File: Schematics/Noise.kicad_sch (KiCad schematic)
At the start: 110 parts, among them J81 Conn_01x02, J82 Conn_01x02, J83 Conn_01x02, J84 Conn_01x02, J85 Conn_01x03, J86 Conn_01x03, J89 Conn_01x03, Q1 2N3904, Q2 BSS138, Q7 BSS138, U126 LM1117-5, U63 TL074, U64 TL072, U65 DG212C, U66 DG212C, U67 TL074, U68 DG212C, U69 DG212C, U70 TL074, U71 PCF8575, U73 LM1117-3.3, U74 TL074, U75 TL074, U76 TL074

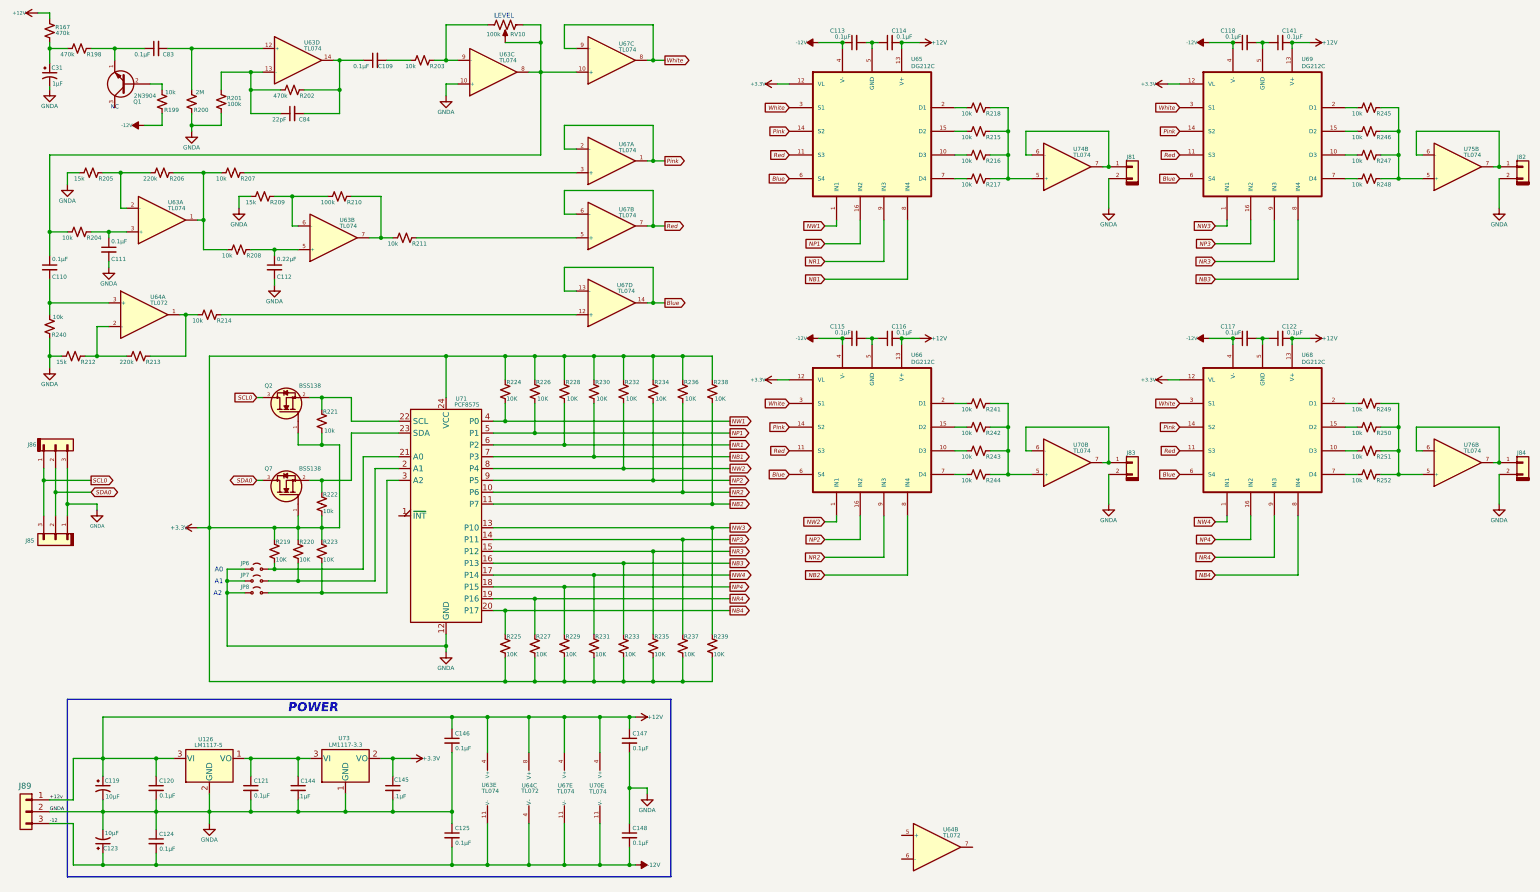
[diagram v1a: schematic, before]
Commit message: Upgreade byte value interface to short.  First stage of refactoring midi input for rotory encoders.  Still needs scaling.
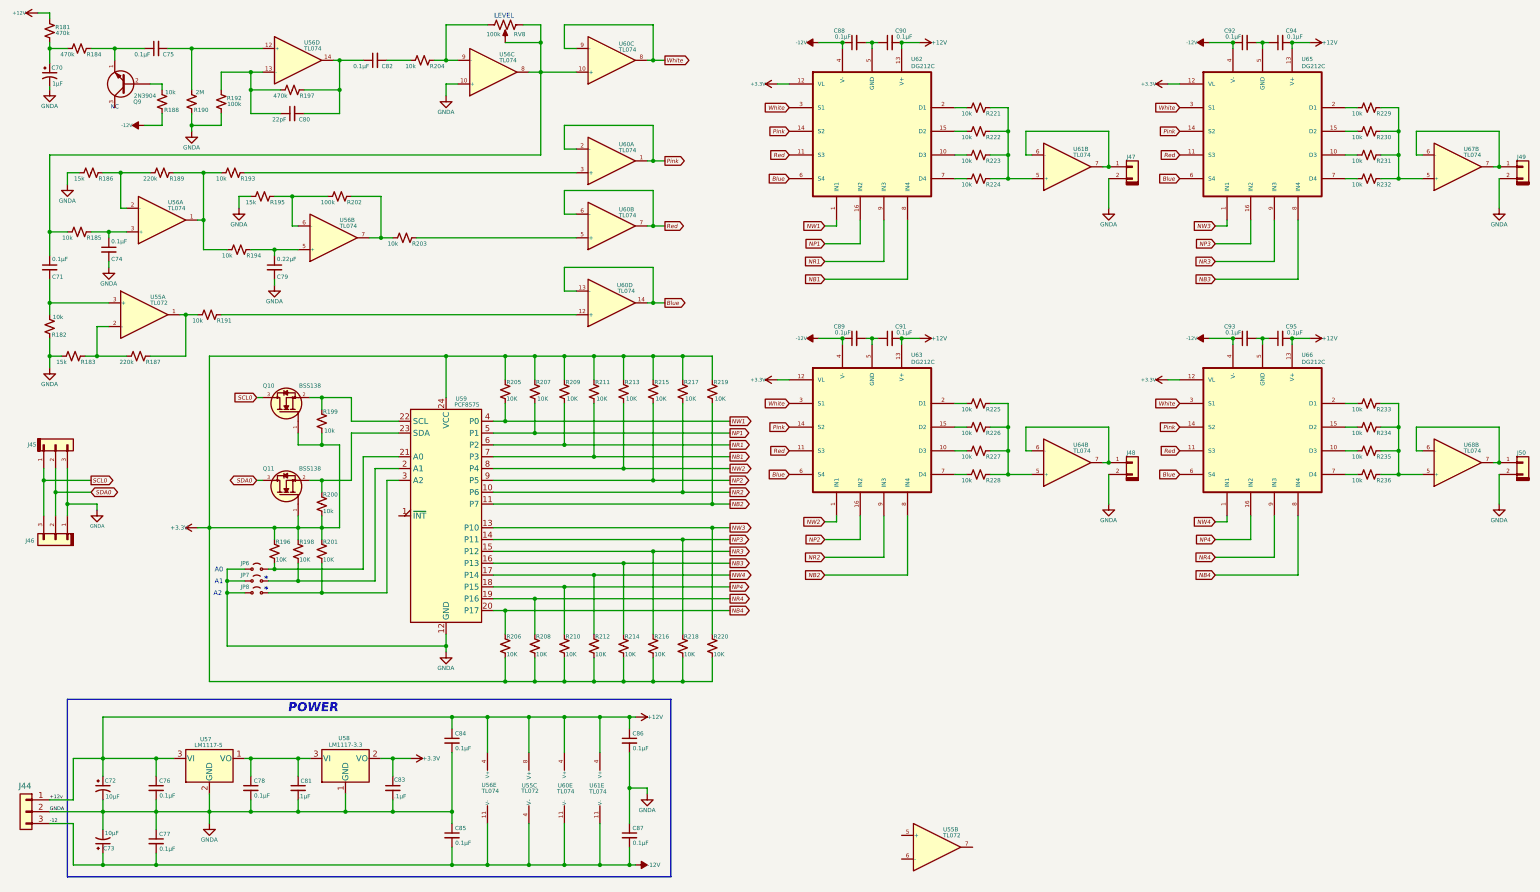
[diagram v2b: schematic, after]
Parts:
- renumbered C31 to C70, C110 to C71, C119 to C72, C123 to C73, C111 to C74, C83 to C75, C120 to C76, C124 to C77, C121 to C78, C112 to C79, C84 to C80, C144 to C81, C109 to C82, C145 to C83, C146 to C84, C125 to C85, C147 to C86, C148 to C87, C113 to C88, C115 to C89, C114 to C90, C116 to C91, C118 to C92, C117 to C93, C141 to C94, C122 to C95, J89 to J44, J86 to J45, J85 to J46, J81 to J47, J83 to J48, J82 to J49, J84 to J50, Q2 to Q10, Q7 to Q11, Q1 to Q9, R167 to R181, R240 to R182, R212 to R183, R198 to R184, R204 to R185, R205 to R186, R213 to R187, R199 to R188, R206 to R189, R200 to R190, R214 to R191, R201 to R192, R207 to R193, R208 to R194, R209 to R195, R219 to R196, R202 to R197, R220 to R198, R221 to R199, R222 to R200, R223 to R201, R210 to R202, R211 to R203, R203 to R204, R224 to R205, R225 to R206, R226 to R207, R227 to R208, R228 to R209, R229 to R210, R230 to R211, R231 to R212, R232 to R213, R233 to R214, R234 to R215, R235 to R216, R236 to R217, R237 to R218, R238 to R219, R239 to R220, R218 to R221, R215 to R222, R216 to R223, R217 to R224, R241 to R225, R242 to R226, R243 to R227, R244 to R228, R245 to R229, R246 to R230, R247 to R231, R248 to R232, R249 to R233, R250 to R234, R251 to R235, R252 to R236, RV10 to RV8, U64 to U55, U63 to U56, U126 to U57, U73 to U58, U71 to U59, U67 to U60, U74 to U61, U70 to U61, U65 to U62, U66 to U63, U70 to U64, U69 to U65, U68 to U66, U75 to U67, U76 to U68
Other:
- note added: "*"

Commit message: Updated schematics including VCO and VCF daughter boards
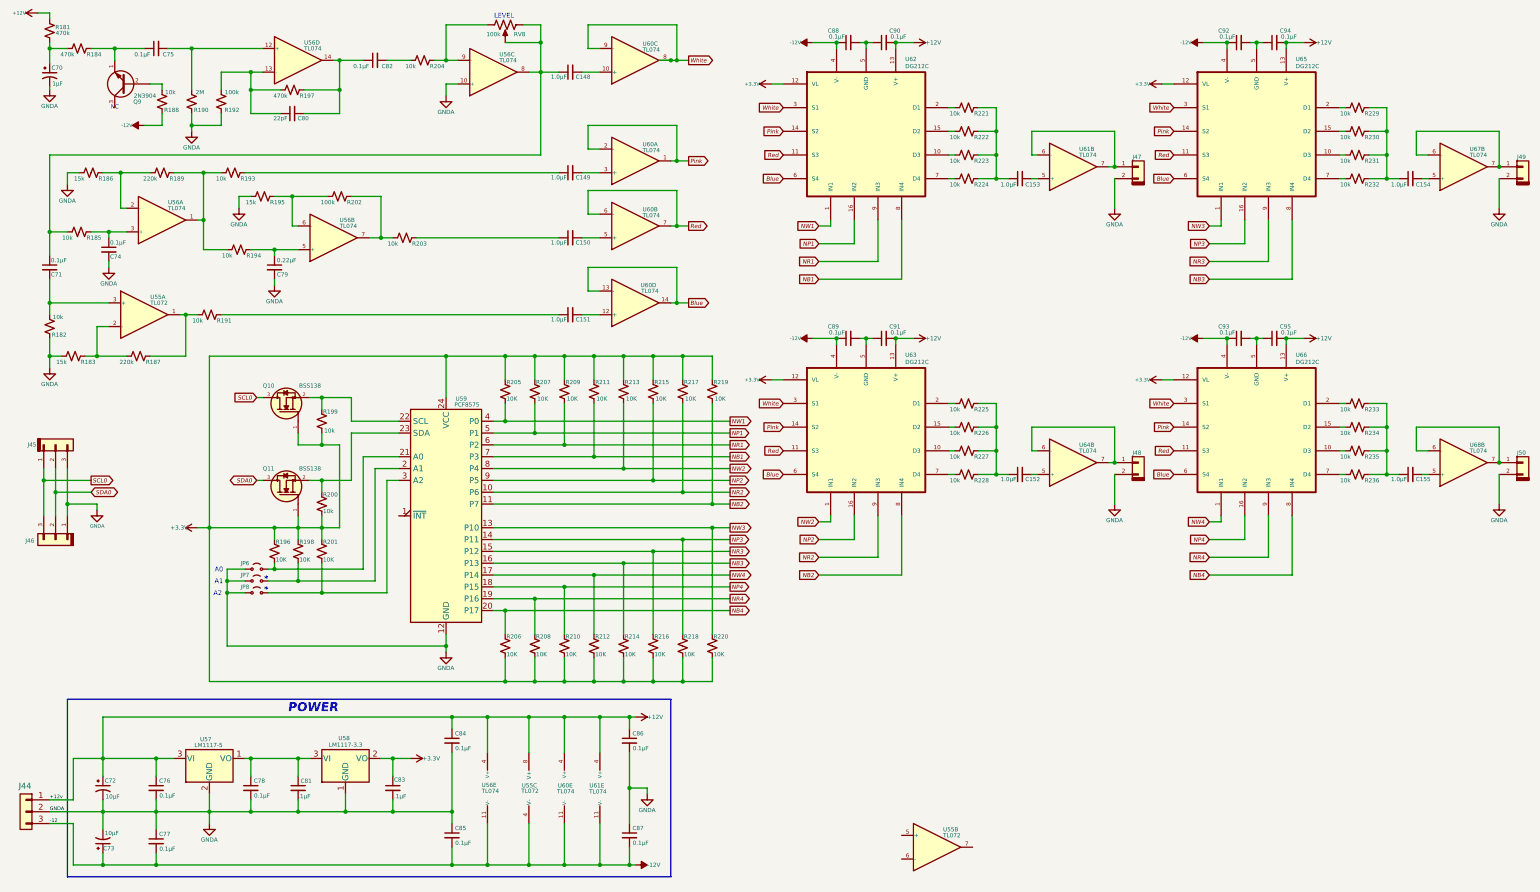
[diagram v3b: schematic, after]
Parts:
- added C148, C149, C150, C151, C152, C153, C154, C155: 1.0µF, symbol Device:C_Small
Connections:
- net at R233.2, R234.2, R235.2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: now also C155.1; no longer U68.5 (+)
- net at R229.2, R230.2, R231.2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: now also C154.1; no longer U67.5 (+)
- net at U60.12 (+): now also C151.2; no longer R191.2
- net at R225.2, R226.2, R227.2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: now also C152.1; no longer U64.5 (+)
- net at R221.2, R222.2, R223.2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: now also C153.1; no longer U61.5 (+)
- net at C71.1, R185.1, RV8. (3)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: now also C148.1; no longer U60.10 (+)
- net at R203.2: now also C150.1; no longer U60.5 (+)
- net at R193.2: now also C149.1; no longer U60.3 (+)
- new net: C152.2, U64.5 (+)
- new net: C149.2, U60.3 (+)
- new net: C155.2, U68.5 (+)
- new net: C154.2, U67.5 (+)
- new net: C153.2, U61.5 (+)
- new net: C150.2, U60.5 (+)
- new net: C148.2, U60.10 (+)
- new net: C151.1, R191.2
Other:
- title: Noise Generator and Multiplexer -> Dual Noise Geneartor
- moved on the sheet: C88, C89, C90, C91, C92, C93, C94, C95, J47, J48, R221, R222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

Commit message: Final tweaks on LFO interfaces and tuning.  Update display layouts.
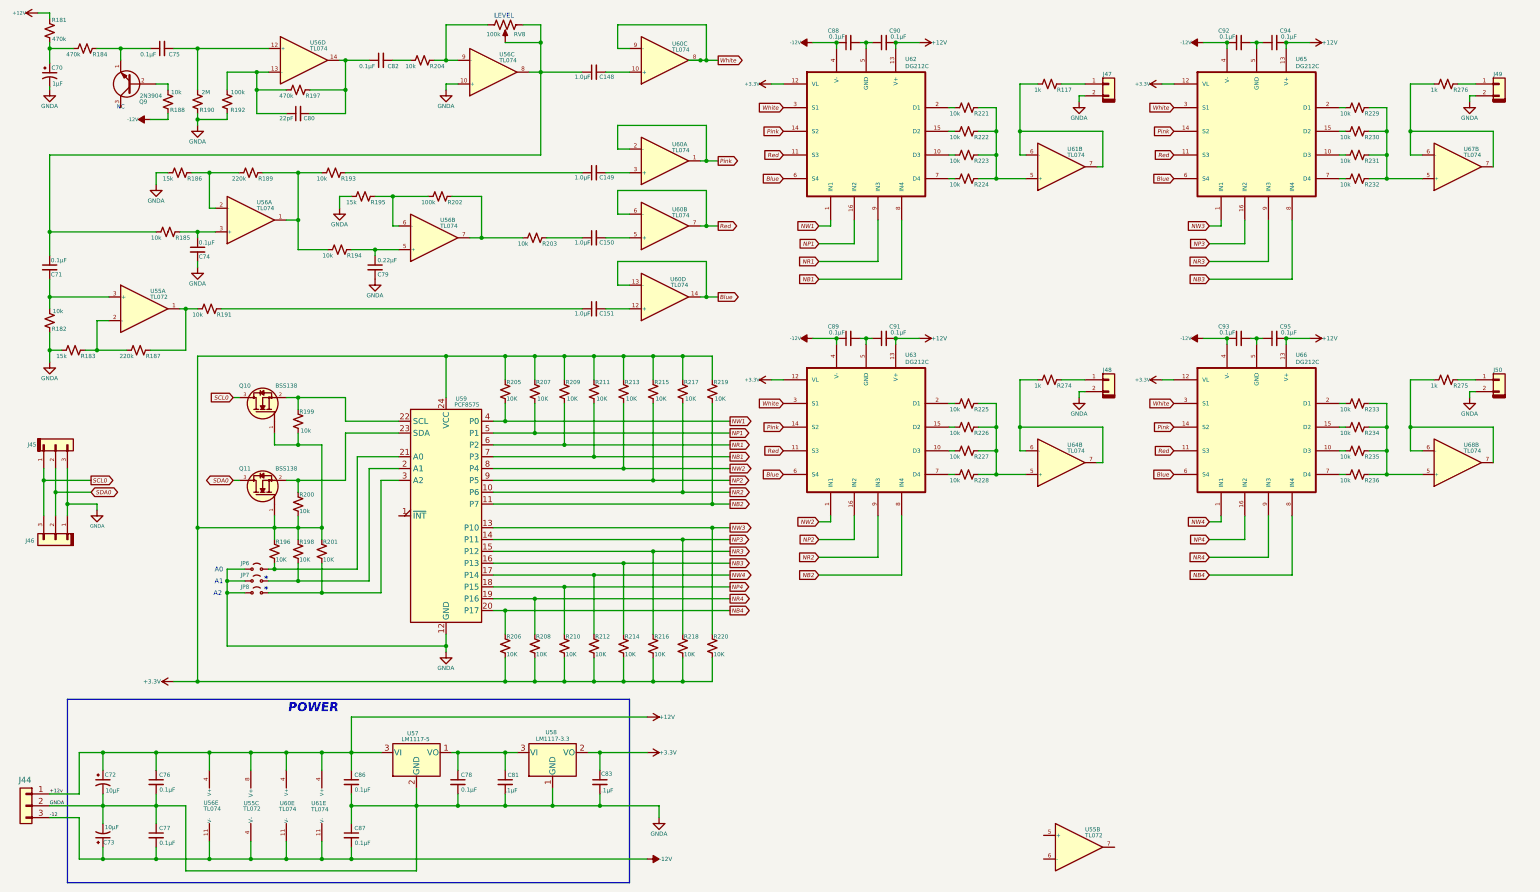
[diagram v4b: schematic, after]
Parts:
- removed C152, C153, C154, C155: 1.0µF, symbol Device:C_Small
- removed C84, C85: 0.1µF, symbol Device:C_Small
- added R117, R274, R275, R276: 1k, symbol Device:R_Small_US
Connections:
- net at R233.2, R234.2, R235.2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: now also U68.5 (+)
- net at R229.2, R230.2, R231.2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: now also U67.5 (+)
- net at R225.2, R226.2, R227.2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: now also U64.5 (+)
- net at U68.6 (-), U68.7: now also R275.1; no longer J50.1 (Pin_1)
- net at R221.2, R222.2, R223.2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: now also U61.5 (+)
- net at U61.6 (-), U61.7: now also R117.1; no longer J47.1 (Pin_1)
- net at U67.6 (-), U67.7: now also R276.1; no longer J49.1 (Pin_1)
- net at U64.6 (-), U64.7: now also R274.1; no longer J48.1 (Pin_1)
- new net: J48.1 (Pin_1), R274.2
- new net: J49.1 (Pin_1), R276.2
- new net: J47.1 (Pin_1), R117.2
- new net: J50.1 (Pin_1), R275.2
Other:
- moved on the sheet: C148, C149, C150, C151, C72, C73, C74, C75, C76, C77, C78, C79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

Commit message: Cleaned up page advance on display controls.
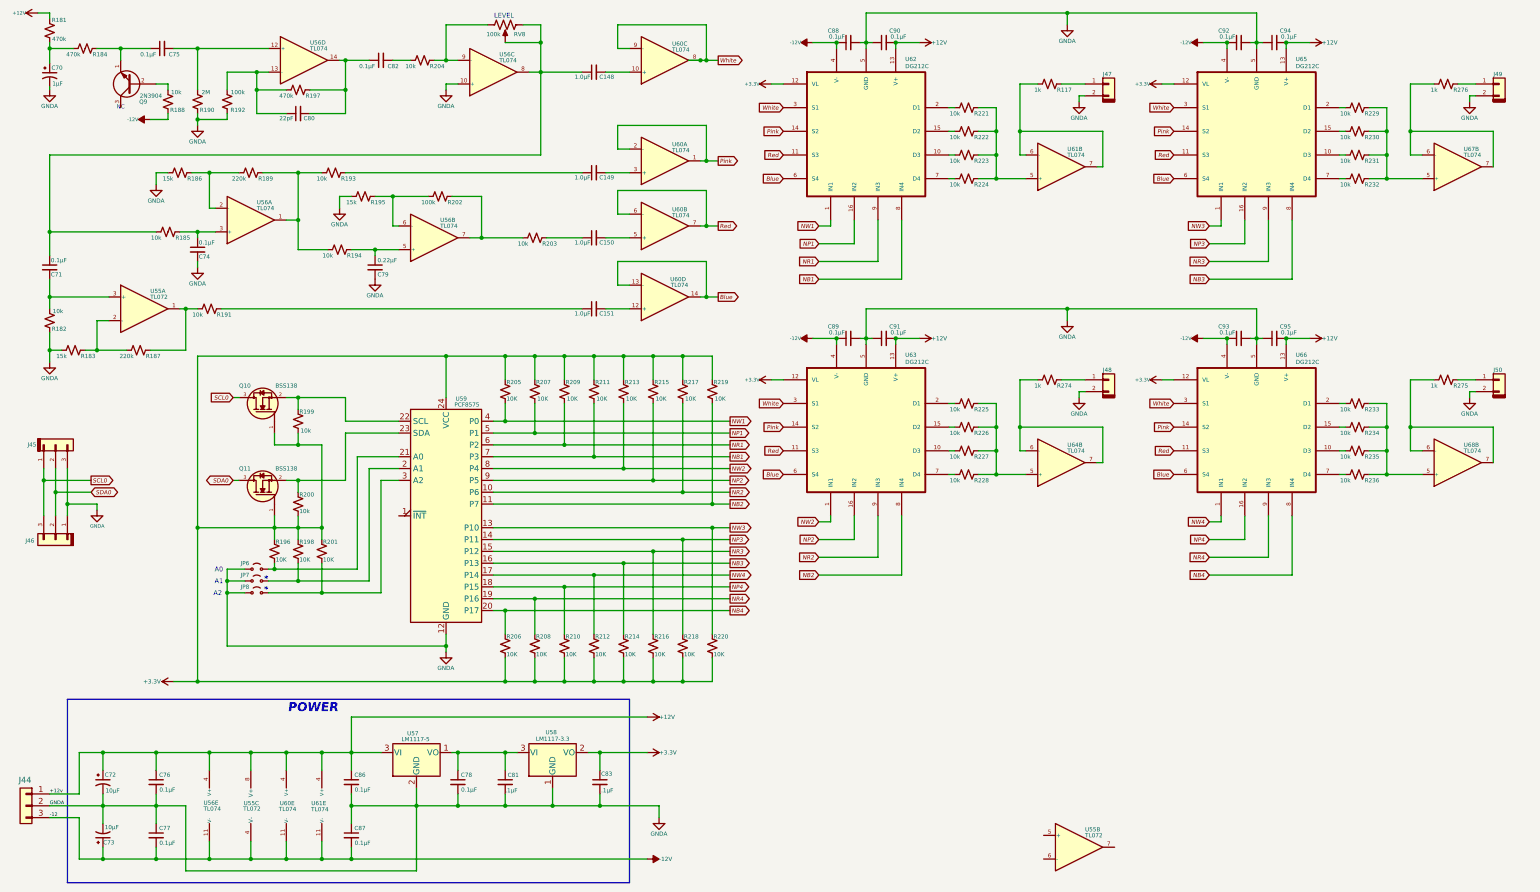
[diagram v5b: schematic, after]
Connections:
- net GNDA: now also C88.2, C89.2, C90.1, C91.1, C92.2, C93.2, C94.1, C95.1, U62.5 (GND), U63.5 (GND), U65.5 (GND), U66.5 (GND)

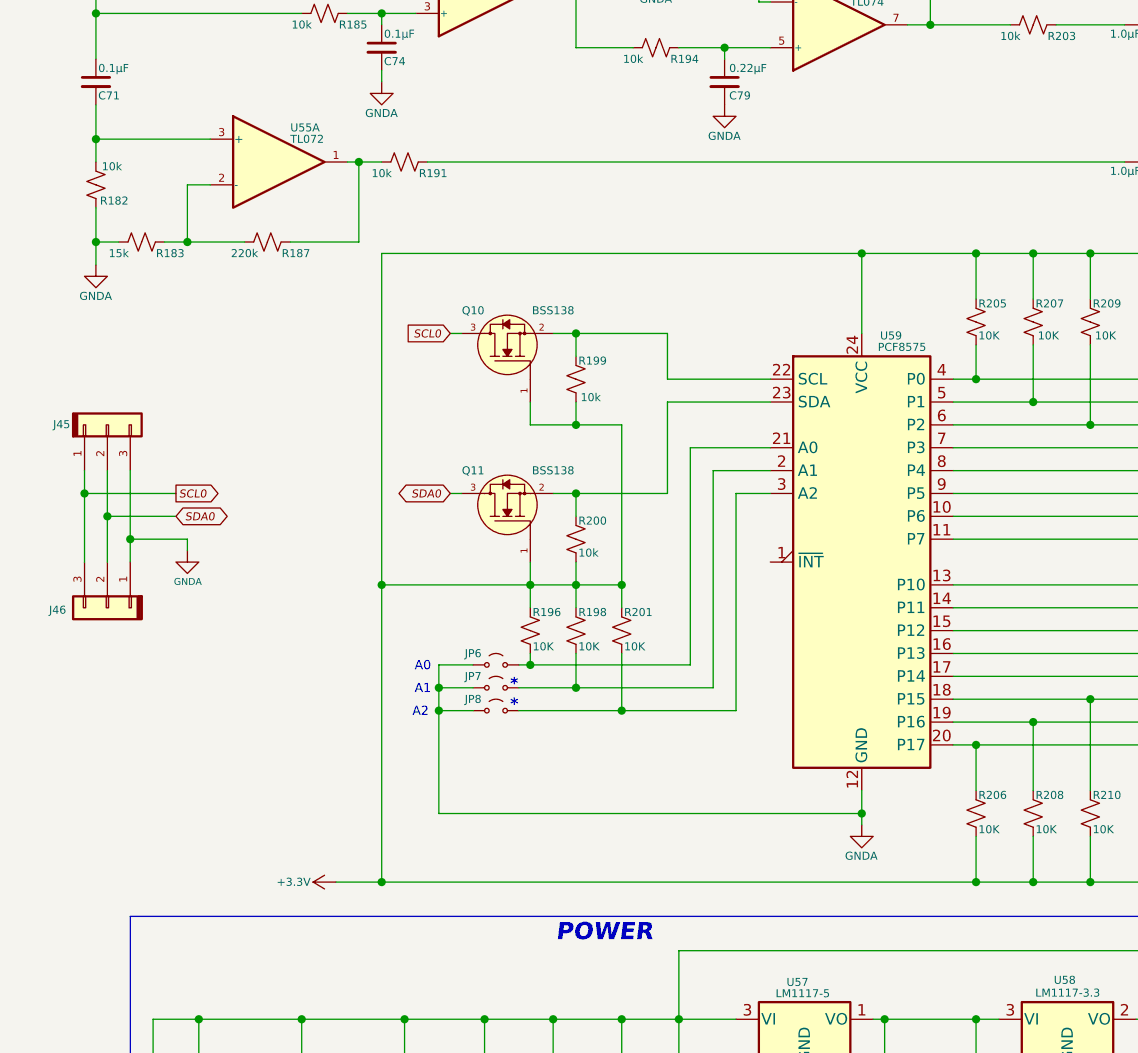
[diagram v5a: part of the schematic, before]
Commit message: minor adjustments for modulation control interface.
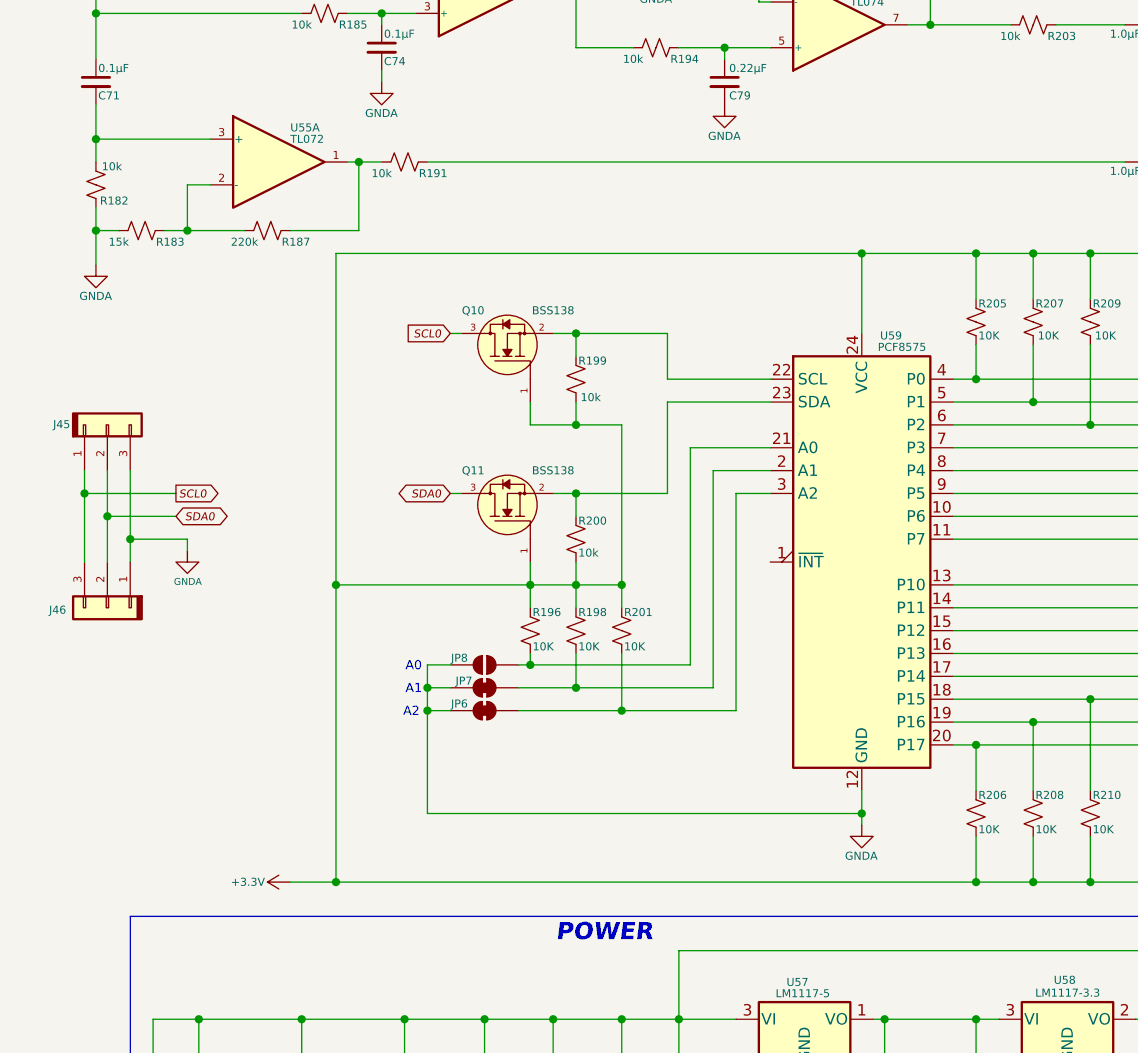
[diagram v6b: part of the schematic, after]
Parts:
- removed JP6, JP7, JP8: Jumper_2_Small_Open, symbol Jumper:Jumper_2_Small_Open
- added JP6, JP7: ~, symbol Jumper:SolderJumper_2_Bridged
- added JP8: SolderJumper_2_Open, symbol Jumper:SolderJumper_2_Open
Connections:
- net GNDA: now also JP6.1 (A), JP7.1 (A), JP8.1 (A)
- net at R196.2, U59.21 (A0): now also JP8.2 (B)
- net at R198.2, U59.2 (A1): now also JP7.2 (B)
- net at R201.2, U59.3 (A2): now also JP6.2 (B)
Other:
- note removed: "*"
- moved on the sheet: R183, R187
